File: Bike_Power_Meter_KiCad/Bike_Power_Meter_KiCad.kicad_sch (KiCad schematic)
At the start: 26 parts, among them J1 USB_C_Receptacle_USB2.0_16P, J2 Conn_01x02_Socket, J3 Conn_01x02_Socket, SW1 Reset, SW2 Boot, U1 ICM-20648, U2 LD1117S33TR_SOT223, U3 ESP32-S2-SOLO

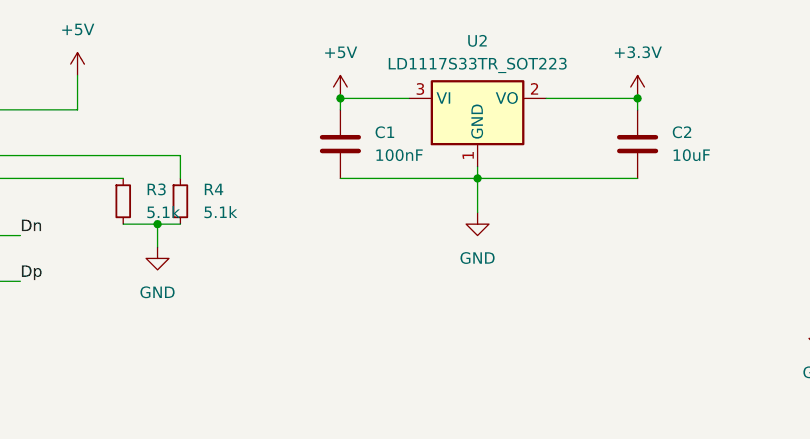
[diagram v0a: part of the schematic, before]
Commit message: changed capacitor unit from nf to uf
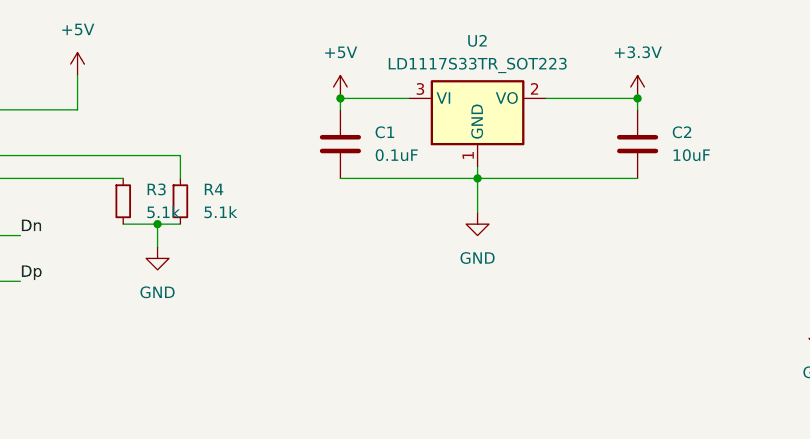
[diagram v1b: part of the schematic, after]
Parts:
- C1: value 100nF -> 0.1uF
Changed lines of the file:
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@@
 			)
 		)
-		(property "Value" "100nF"
+		(property "Value" "0.1uF"
 			(at 88.9 27.9399 0)
 			(effects
